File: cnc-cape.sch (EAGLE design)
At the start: 122 parts, among them IC1 LM2576hvt, IC2 74HC14N, IC3 74HC14N, IC4 74HCT244N, IC5 74HCT244N, IC6 74HC14N, IC7 LM1458N, J1 22-27-2041-04, J10 22-27-2031-03, J11 22-27-2031-03, J12 22-27-2031-03, J13 22-27-2031-03, J14 22-27-2031-03, J15 22-27-2031-03, J16 22-27-2031-03, J17 22-27-2031-03, J18 22-27-2031-03, J19 22-27-2031-03, J2 22-27-2041-04, J20 22-27-2031-03, J21 22-27-2031-03, J22 22-27-2031-03, J3 22-27-2041-04, J4 22-27-2041-04, J5 22-27-2041-04, J6 22-27-2031-03, J7 22-27-2031-03, J8 22-27-2031-03, J9 22-27-2031-03, K1 G2R2, K2 G2R2, K3 G2R2, Q1 2N7000, Q2 2N7000, T1 1n2222, T2 1n2222, T3 1n2222, X5 Power In

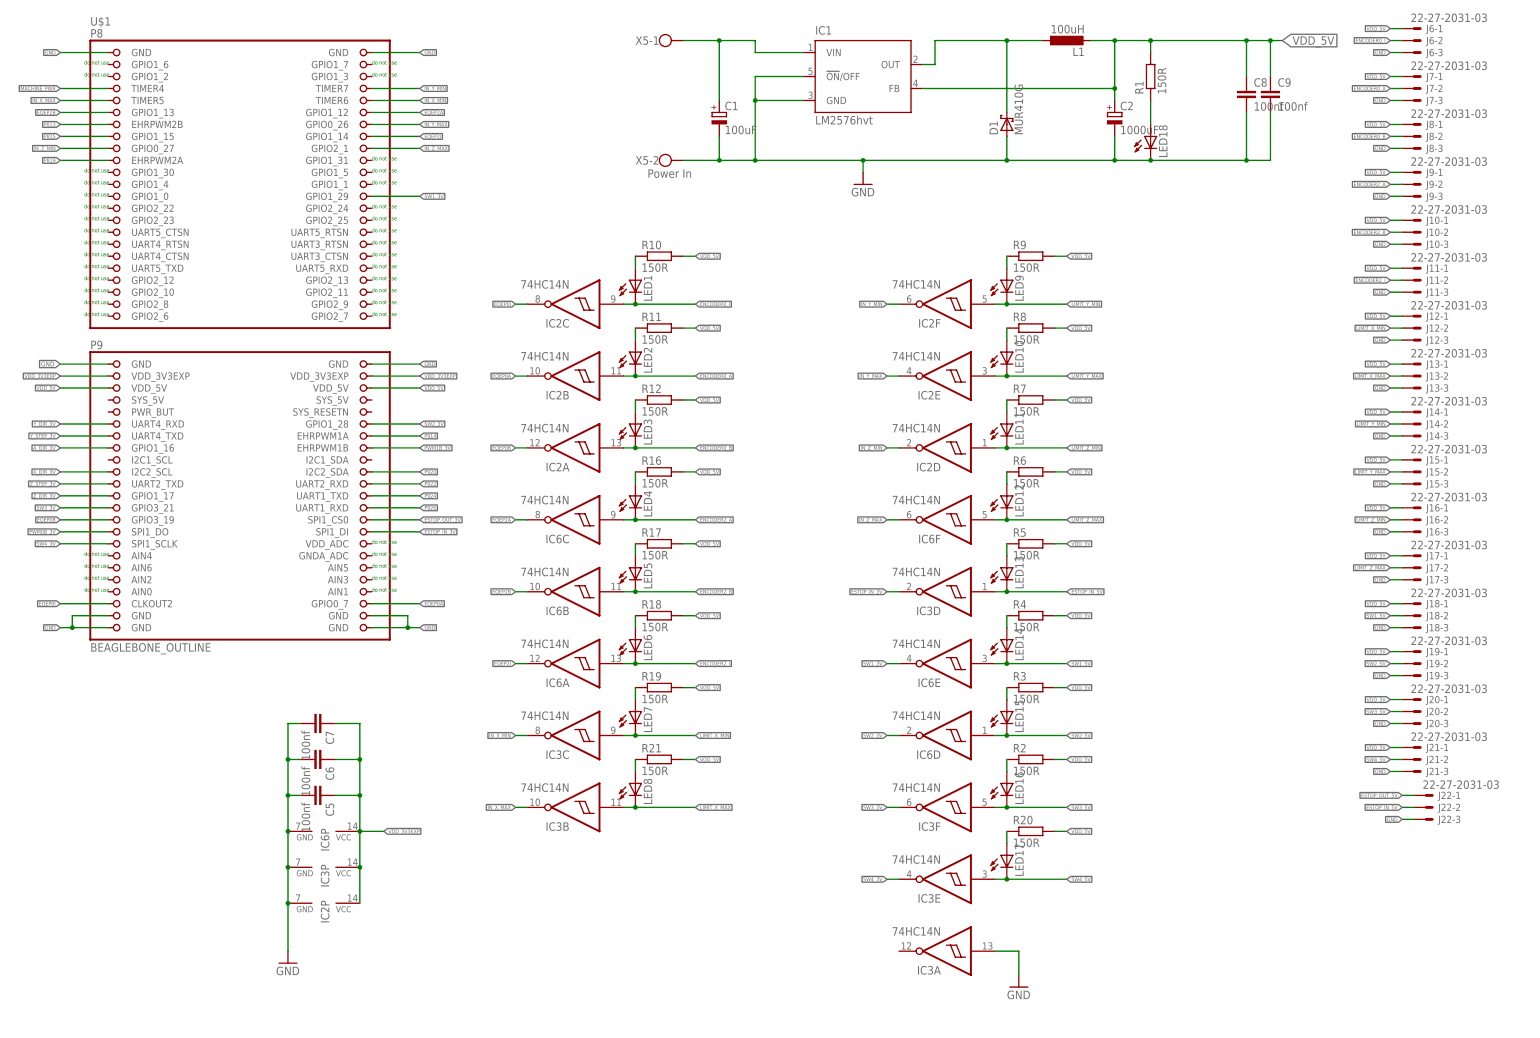
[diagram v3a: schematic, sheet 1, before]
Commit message: fixed some net names
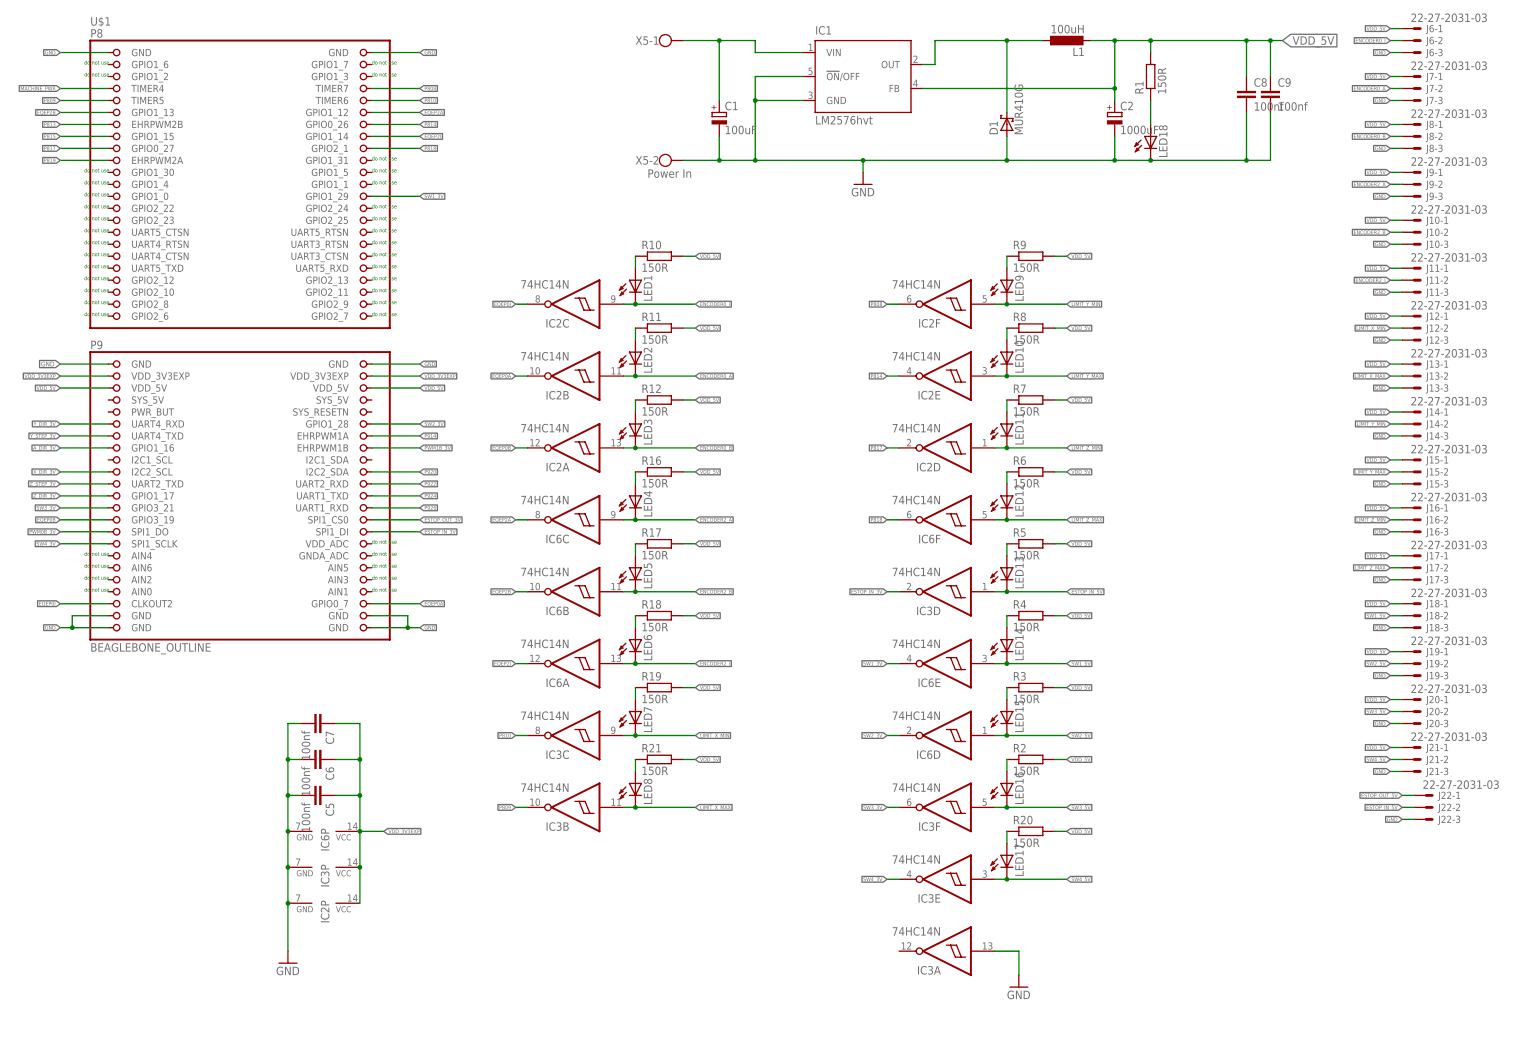
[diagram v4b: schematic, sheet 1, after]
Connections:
- net IN_X_MAX renamed P809
- net IN_X_MIN renamed P810
- net IN_Y_MAX renamed P814
- net IN_Y_MIN renamed P808
- net IN_Z_MAX renamed P818
- net IN_Z_MIN renamed P817
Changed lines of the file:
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@@
 </segment>
 </net>
-<net name="IN_X_MIN" class="0">
+<net name="P810" class="0">
 <segment>
 <wire x1="-43.18" y1="-20.32" x2="-45.72" y2="-20.32" width="0.1524" layer="91"/>
@@
 </segment>
 </net>
-<net name="IN_X_MAX" class="0">
+<net name="P809" class="0">
 <segment>
 <wire x1="-43.18" y1="-35.56" x2="-45.72" y2="-35.56" width="0.1524" layer="91"/>
@@
 </segment>
 </net>
-<net name="IN_Y_MIN" class="0">
+<net name="P808" class="0">
 <segment>
 <wire x1="35.56" y1="71.12" x2="33.02" y2="71.12" width="0.1524" layer="91"/>
@@
 </segment>
 </net>
-<net name="IN_Y_MAX" class="0">
+<net name="P814" class="0">
 <segment>
 <wire x1="35.56" y1="55.88" x2="33.02" y2="55.88" width="0.1524" layer="91"/>
@@
 </segment>
 </net>
-<net name="IN_Z_MIN" class="0">
+<net name="P817" class="0">
 <segment>
 <wire x1="35.56" y1="40.64" x2="33.02" y2="40.64" width="0.1524" layer="91"/>
@@
 </segment>
 </net>
-<net name="IN_Z_MAX" class="0">
+<net name="P818" class="0">
 <segment>
 <wire x1="35.56" y1="25.4" x2="33.02" y2="25.4" width="0.1524" layer="91"/>
